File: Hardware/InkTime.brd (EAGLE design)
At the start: 46 x 35 mm, 105 parts, among them IC1 BQ25180YBGR_BQ25180YBGR, IC2 BMA423, IC3 DRV2605YZFR, IC9 RT6160AWSC, J1 TC2030-IDC_TC2030-IDC, J2 503480-2400_503480-2400, J3 KH-TYPE-C-16P, Q1 ESP32_C6_LIBRARY_4_ESP32_WROV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, Q3 SI1308EDL-T1-GE3, U1 MAX17048G+T10, X1 32MHz, X2 32.768kHz

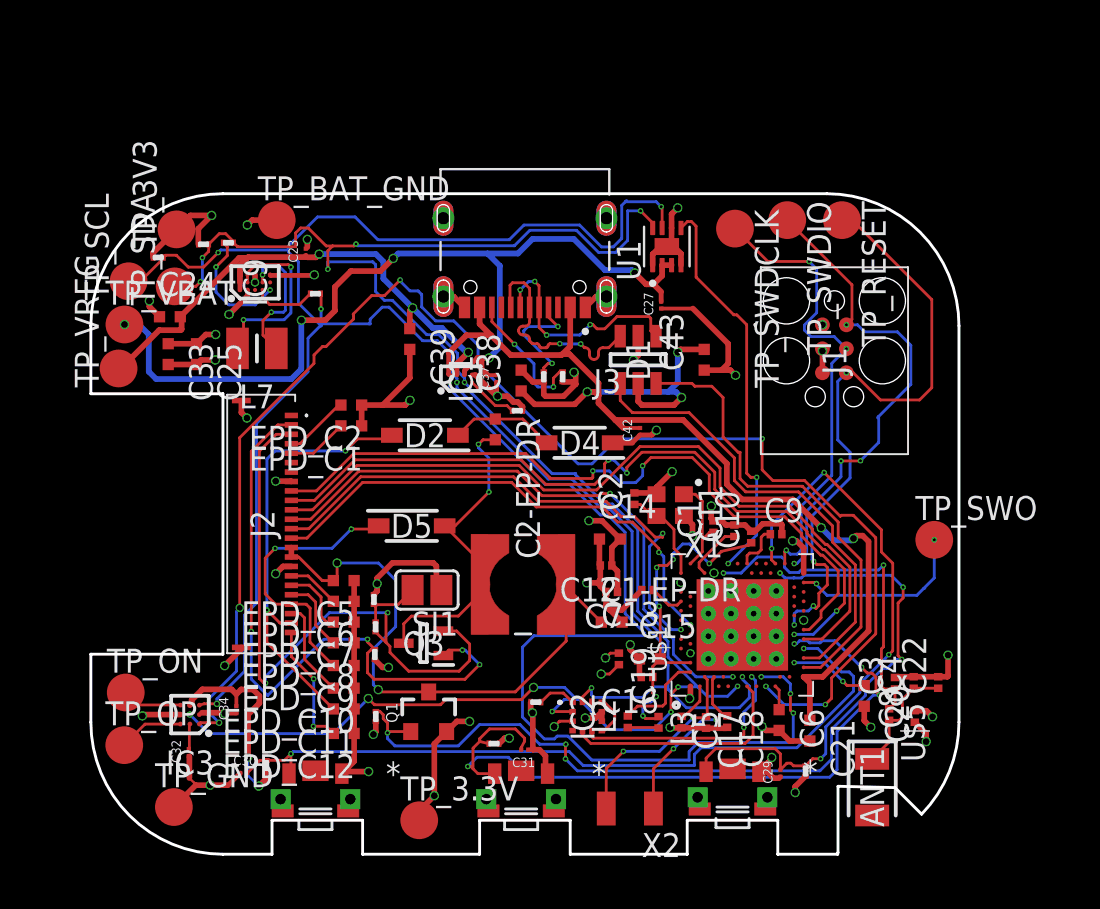
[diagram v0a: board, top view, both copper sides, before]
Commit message: fixed: issue 1, 2 and 3
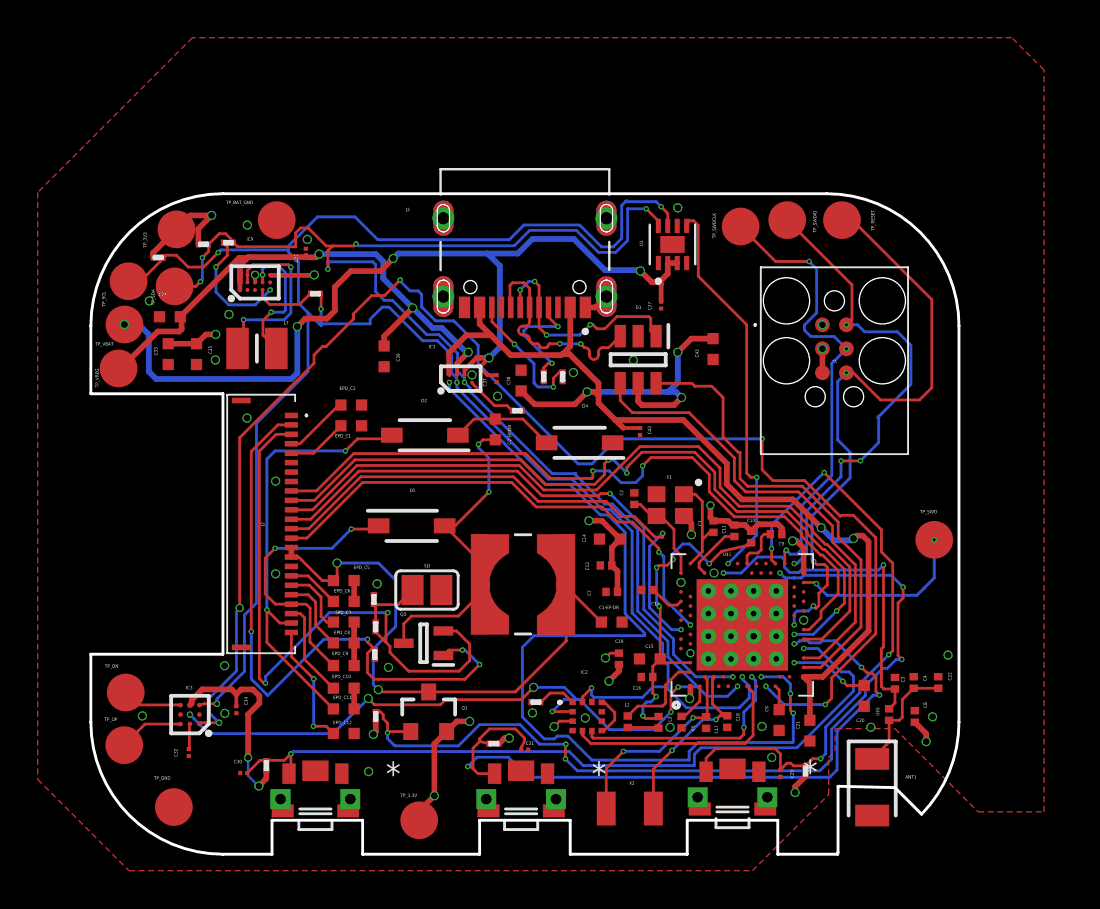
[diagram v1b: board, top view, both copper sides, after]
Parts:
- moved C39 1.64 mm to (-7.46, 8.88)
- moved C43 0.74 mm to (9.97, 9.27)
- moved U1 0.32 mm to (7.82, 14.8)
- moved TP_SWDCLK 0.32 mm to (11.4, 15.8)
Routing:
- net GND: track 121.1 -> 15.9 mm, vias 40 -> 35
- net VREG: track 28.9 -> 30.3 mm
- net VBUS: track 64.5 -> 65.2 mm
- added copper zone on layer 1, net GND
